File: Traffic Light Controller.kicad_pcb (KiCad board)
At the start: 2 copper layers, 107.5 x 82.5 mm, 65 parts, among them J1 Conn_02x08_Odd_Even, J2 Conn_02x08_Odd_Even, J3 Conn_02x05_Odd_Even, J4 +5V, SW1 RST, SW2 OVR, SW3 EN, U1 SM420561N, U2 SM420561N, U3 LM1117DT-3.3

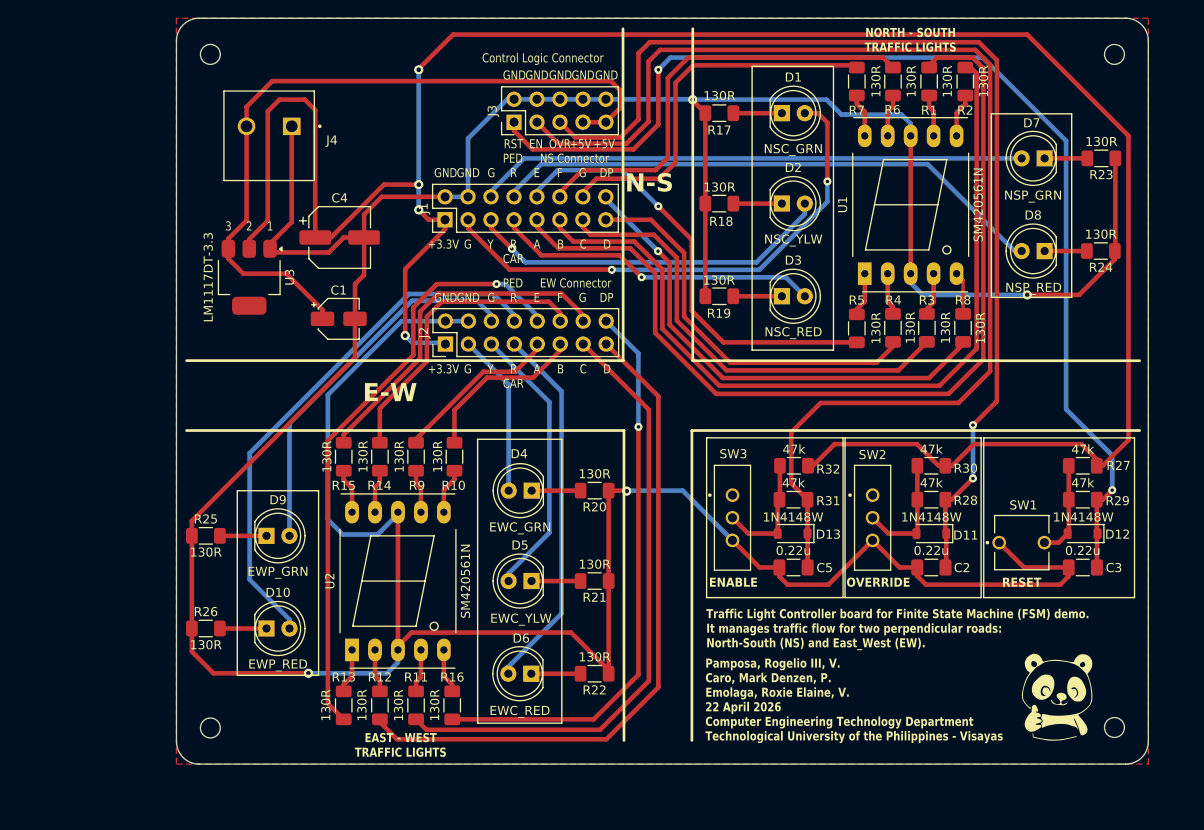
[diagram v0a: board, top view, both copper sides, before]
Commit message: converted to 9.0 version
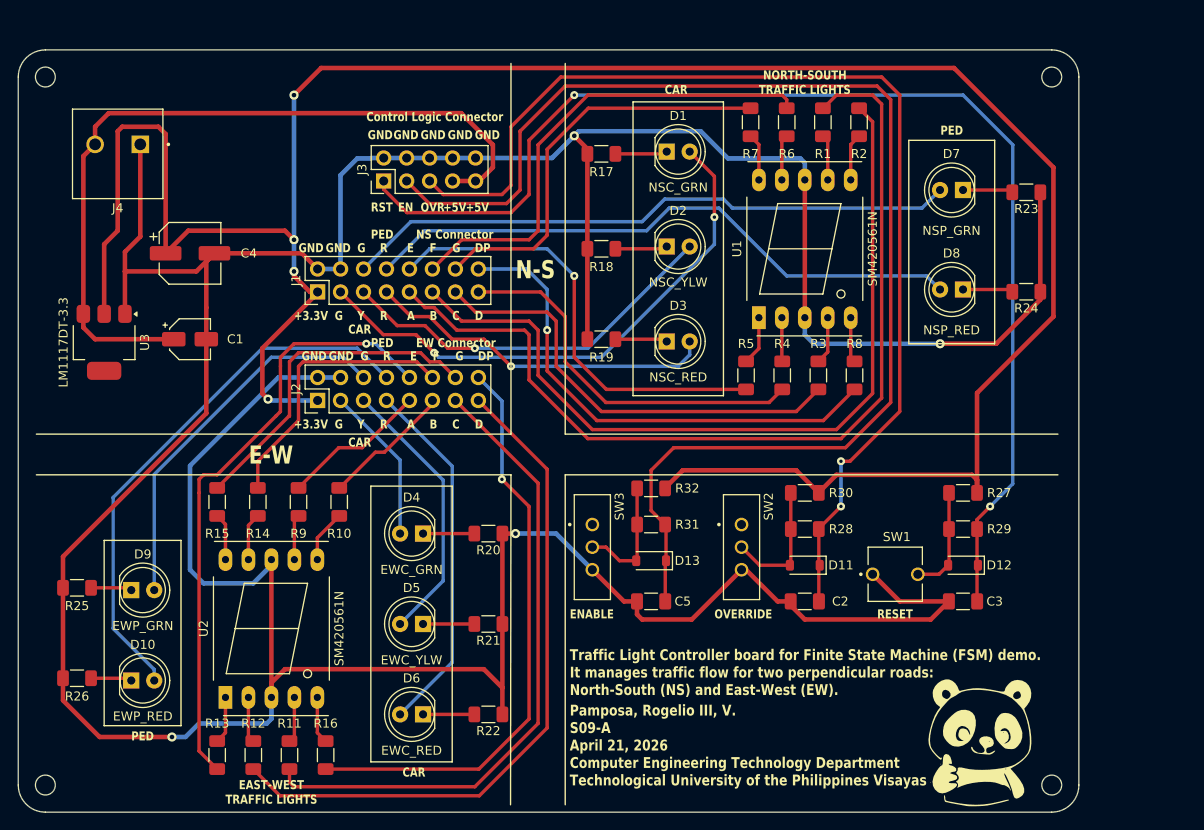
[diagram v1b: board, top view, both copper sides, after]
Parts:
- R27, R28, R29, R30, R31, R32: value 47k -> 47K
- moved H4 82.8 mm to (79.0, 138.8)
- moved H3 81.1 mm to (190.3, 138.8)
- moved H1 74.3 mm to (79.0, 60.5)
- moved H2 72.3 mm to (190.3, 60.5)
- moved U3 17.6 mm to (85.5, 89.8)
- moved J4 16.9 mm to (87.0, 68.0)
- moved C4 16.6 mm to (95.0, 80.0)
- moved C1 16.6 mm to (95.0, 89.5)
- moved J1 16.2 mm to (109.1, 84.3)
- moved C5 16.2 mm to (146.0, 118.5)
- moved D9 16.1 mm to (88.5, 117.2)
- moved D10 16.0 mm to (88.5, 127.2)
- moved R32 16.0 mm to (146.0, 106.0)
- moved R31 16.0 mm to (146.0, 110.0), turned to 0 degrees
- moved D13 15.9 mm to (146.0, 114.0)
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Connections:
- R27 pad 1: Net-(D12-A) -> /+3.3V
- R27 pad 2: /+3.3V -> Net-(D12-A)
- R28 pad 1: /OVR -> Net-(D11-A)
- R28 pad 2: Net-(D11-A) -> /OVR
- R31 pad 1: /EN -> Net-(D13-A)
- R31 pad 2: Net-(D13-A) -> /EN
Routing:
- net GND: track 429.3 -> 453.5 mm
- net /+3.3V: track 248.1 -> 267.3 mm
- net /RST: track 124.9 -> 134.9 mm
- net /EN: track 134.4 -> 142.7 mm
- net /NSP_GRN: track 60.8 -> 68.2 mm
- net /+5V: track 81.0 -> 86.9 mm
- net /NSP_RED: track 62.0 -> 67.7 mm
- net /OVR: track 117.5 -> 122.9 mm
- net /NS_HEX_F: track 49.1 -> 53.9 mm
- net /EW_HEX_B: track 18.7 -> 14.6 mm
- net /NS_HEX_G: track 41.9 -> 45.6 mm
- net /NSC_GRN: track 57.4 -> 60.9 mm
- net /EW_HEX_C: track 68.7 -> 71.6 mm
- net /NSC_YLW: track 40.6 -> 43.3 mm
- net /NSC_RED: track 36.2 -> 39.0 mm
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- removed copper zone on F.Cu, net (none)
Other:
- board size 107.5 x 82.5 mm -> 117.3 x 84.3 mm
- board text added: "EAST-WEST TRAFFIC LIGHTS"
- board text added: "NORTH-SOUTH TRAFFIC LIGHTS"
- board text added: "Pamposa, Rogelio III, V. S09-A April 21, 2026 Computer Engineering Technology Department Technological University of the Philippines Visayas"
- board text added: "Traffic Light Controller board for Finite State Machine (FSM) demo. It manages traffic flow for two perpendicular roads: North-South (NS) and East-West (EW)."
- board text removed: "1"
- board text removed: "2"
- board text removed: "3"
- board text removed: "EAST - WEST TRAFFIC LIGHTS"
- board text removed: "NORTH - SOUTH TRAFFIC LIGHTS"
- board text removed: "Pamposa, Rogelio III, V. Caro, Mark Denzen, P. Emolaga, Roxie Elaine, V. 22 April 2026 Computer Engineering Technology Department Technological University of the Philippines - Visayas"
- board text removed: "Traffic Light Controller board for Finite State Machine (FSM) demo. It manages traffic flow for two perpendicular roads: North-South (NS) and East_West (EW)."
